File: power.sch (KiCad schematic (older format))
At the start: 14 parts

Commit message: Bom
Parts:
- removed BT?: Battery, symbol Battery
- C1: renamed from C?; footprint (none) -> Capacitors_SMD:C_1210
- C2: renamed from C?; value 100n 10V -> 100n 100V; footprint Capacitors_SMD:C_0402 -> Capacitors_SMD:C_0805; Rating 10V -> 100V
- C3: renamed from C?; footprint (none) -> Capacitors_SMD:C_1206
- D3: renamed from D?; footprint (none) -> Diodes_SMD:SOD-123
- R2: renamed from R?; footprint (none) -> Resistors_SMD:R_0402
- R3: renamed from R?; value 28k -> 28k 1%; footprint (none) -> Resistors_SMD:R_0402
- R4: renamed from R?; value 8.45k -> 8.45k 1%; footprint (none) -> Resistors_SMD:R_0402
- gave numbers to parts that had none: 6
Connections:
- net labels removed: VBAT
- wire segments 33 -> 31
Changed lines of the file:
@@
 $EndDescr
 $Comp
-L VIN #PWR?
+L VIN #PWR01
 U 1 1 562BB258
 P 750 1250
-F 0 "#PWR?" H 750 1100 50  0001 C CNN
+F 0 "#PWR01" H 750 1100 50  0001 C CNN
 F 1 "VIN" H 750 1390 50  0000 C CNN
 F 2 "" H 750 1250 60  0000 C CNN
@@
 24 V
 $Comp
-L R R?
+L R R1
 U 1 1 5637DBF2
 P 1200 2450
-F 0 "R?" V 1280 2450 50  0000 C CNN
+F 0 "R1" V 1280 2450 50  0000 C CNN
 F 1 "100k" V 1200 2450 50  0000 C CNN
 F 2 "Resistors_SMD:R_1206" V 1130 2450 30  0001 C CNN
@@
 $EndComp
 $Comp
-L GND #PWR?
+L GND #PWR02
 U 1 1 5637DBF8
 P 1200 2900
-F 0 "#PWR?" H 1200 2650 50  0001 C CNN
+F 0 "#PWR02" H 1200 2650 50  0001 C CNN
 F 1 "GND" H 1200 2750 50  0000 C CNN
 F 2 "" H 1200 2900 60  0000 C CNN
@@
 $EndComp
 $Comp
-L ZENER D?
+L ZENER D2
 U 1 1 5637E04D
 P 1600 1750
-F 0 "D?" H 1600 1850 50  0000 C CNN
+F 0 "D2" H 1600 1850 50  0000 C CNN
 F 1 "10V" H 1600 1650 50  0000 C CNN
 F 2 "Diodes_SMD:SMA_Standard" H 1600 1750 60  0001 C CNN
@@
 $EndComp
 $Comp
-L Battery BT?
-U 1 1 57AF2EDA
-P 2650 6400
-F 0 "BT?" H 2768 6446 50  0000 L CNN
-F 1 "Battery" H 2768 6355 50  0000 L CNN
-F 2 "" V 2650 6440 50  0001 C CNN
-F 3 "" V 2650 6440 50  0000 C CNN
-	1    2650 6400
-	1    0    0    -1
-$EndComp
-$Comp
-L VBAT #PWR?
-U 1 1 57AF30BC
-P 2650 6000
-F 0 "#PWR?" H 2650 5850 50  0001 C CNN
-F 1 "VBAT" H 2650 6140 50  0000 C CNN
-F 2 "" H 2650 6000 60  0000 C CNN
-F 3 "" H 2650 6000 60  0000 C CNN
-	1    2650 6000
-	1    0    0    -1
-$EndComp
-$Comp
-L GND #PWR?
-U 1 1 57AF3133
-P 2650 6800
-F 0 "#PWR?" H 2650 6550 50  0001 C CNN
-F 1 "GND" H 2650 6650 50  0000 C CNN
-F 2 "" H 2650 6800 60  0000 C CNN
-F 3 "" H 2650 6800 60  0000 C CNN
-	1    2650 6800
-	1    0    0    -1
-$EndComp
-$Comp
-L TVS D?
+L TVS D1
 U 1 1 57AF3BB5
 P 850 2200
-F 0 "D?" V 804 2288 50  0000 L CNN
+F 0 "D1" V 804 2288 50  0000 L CNN
 F 1 "40.2V" V 895 2288 50  0000 L CNN
 F 2 "can-node:DO-214AC" H 850 2200 50  0001 C CNN
@@
 $EndComp
 $Comp
-L GND #PWR?
+L GND #PWR03
 U 1 1 57AF3EE9
 P 850 2900
-F 0 "#PWR?" H 850 2650 50  0001 C CNN
+F 0 "#PWR03" H 850 2650 50  0001 C CNN
 F 1 "GND" H 850 2750 50  0000 C CNN
 F 2 "" H 850 2900 60  0000 C CNN
@@
 	750  1400 950  1400
 Wire Wire Line
-	2650 6000 2650 6250
-Wire Wire Line
-	2650 6550 2650 6800
-Wire Wire Line
 	850  1900 850  1400
 Connection ~ 850  1400
@@
 	1350 1400 2900 1400
 $Comp
-L GND #PWR?
+L GND #PWR04
 U 1 1 57C23EF3
 P 4350 5750
-F 0 "#PWR?" H 4350 5500 50  0001 C CNN
+F 0 "#PWR04" H 4350 5500 50  0001 C CNN
 F 1 "GND" H 4350 5600 50  0000 C CNN
 F 2 "" H 4350 5750 60  0000 C CNN
@@
 $EndComp
 $Comp
-L GNDA #PWR?
+L GNDA #PWR05
 U 1 1 57C23EF9
 P 4700 5750
-F 0 "#PWR?" H 4700 5500 50  0001 C CNN
+F 0 "#PWR05" H 4700 5500 50  0001 C CNN
 F 1 "GNDA" H 4700 5600 50  0000 C CNN
 F 2 "" H 4700 5750 60  0000 C CNN
@@
 	4350 5750 4700 5750
 $Comp
-L +3.3V #PWR?
+L +3.3V #PWR06
 U 1 1 57C23F59
 P 4350 5400
-F 0 "#PWR?" H 4350 5250 50  0001 C CNN
+F 0 "#PWR06" H 4350 5250 50  0001 C CNN
 F 1 "+3.3V" H 4365 5573 50  0000 C CNN
 F 2 "" H 4350 5400 50  0000 C CNN
@@
 $EndComp
 $Comp
-L +3.3VADC #PWR?
+L +3.3VADC #PWR07
 U 1 1 57C23F9D
 P 4700 5400
-F 0 "#PWR?" H 4850 5350 50  0001 C CNN
+F 0 "#PWR07" H 4850 5350 50  0001 C CNN
 F 1 "+3.3VADC" H 4720 5543 50  0000 C CNN
 F 2 "" H 4700 5400 50  0000 C CNN
@@
 	4700 5450 4700 5400
 $Comp
-L DMP6023LSS Q?
+L DMP6023LSS Q1
 U 1 1 57C95065
 P 1150 1500
-F 0 "Q?" V 1450 1500 50  0000 C CNN
+F 0 "Q1" V 1450 1500 50  0000 C CNN
 F 1 "DMP6023LSS" V 1350 1500 50  0000 C CNN
 F 2 "can-node:DMP6023LSS" V 1100 1750 50  0001 C CIN
@@
 $EndComp
 $Comp
-L LMR16006 U?
+L LMR16006 U1
 U 1 1 57D41661
 P 3300 1700
-F 0 "U?" H 3300 2287 60  0000 C CNN
+F 0 "U1" H 3300 2287 60  0000 C CNN
 F 1 "LMR16006" H 3300 2181 60  0000 C CNN
-F 2 "" H 3300 1600 60  0000 C CNN
+F 2 "" H 3300 1600 60  0001 C CNN
 F 3 "" H 3300 1600 60  0000 C CNN
 	1    3300 1700
@@
 $EndComp
 $Comp
-L C C?
+L C C2
 U 1 1 57D41A9C
 P 3950 1400
-F 0 "C?" V 3698 1400 50  0000 C CNN
-F 1 "100n 10V" V 3789 1400 50  0000 C CNN
-F 2 "Capacitors_SMD:C_0402" H 3988 1250 50  0001 C CNN
+F 0 "C2" V 3698 1400 50  0000 C CNN
+F 1 "100n 100V" V 3789 1400 50  0000 C CNN
+F 2 "Capacitors_SMD:C_0805" H 3988 1250 50  0001 C CNN
 F 3 "" H 3950 1400 50  0000 C CNN
-F 4 "10V" V 3950 1400 60  0001 C CNN "Rating"
+F 4 "100V" V 3950 1400 60  0001 C CNN "Rating"
 	1    3950 1400
 	0    1    1    0
 $EndComp
 $Comp
-L D_Schottky D?
+L D_Schottky D3
 U 1 1 57D41C33
 P 4150 1800
-F 0 "D?" V 4104 1879 50  0000 L CNN
+F 0 "D3" V 4104 1879 50  0000 L CNN
 F 1 "0.57V 1A" V 4195 1879 50  0000 L CNN
-F 2 "" H 4150 1800 50  0000 C CNN
+F 2 "Diodes_SMD:SOD-123" H 4150 1800 50  0001 C CNN
 F 3 "" H 4150 1800 50  0000 C CNN
 	1    4150 1800
@@
 $EndComp
 $Comp
-L INDUCTOR L?
+L INDUCTOR L1
 U 1 1 57D41D41
 P 4550 1600
-F 0 "L?" V 4766 1600 50  0000 C CNN
+F 0 "L1" V 4766 1600 50  0000 C CNN
 F 1 "27µH 220mΩ" V 4675 1600 50  0000 C CNN
-F 2 "" H 4550 1600 50  0000 C CNN
+F 2 "" H 4550 1600 50  0001 C CNN
 F 3 "" H 4550 1600 50  0000 C CNN
 	1    4550 1600
@@
 $EndComp
 $Comp
-L C C?
+L C C3
 U 1 1 57D41E1E
 P 5350 1900
-F 0 "C?" H 5465 1946 50  0000 L CNN
+F 0 "C3" H 5465 1946 50  0000 L CNN
 F 1 "22µF" H 5465 1855 50  0000 L CNN
-F 2 "" H 5388 1750 50  0000 C CNN
+F 2 "Capacitors_SMD:C_1206" H 5388 1750 50  0001 C CNN
 F 3 "" H 5350 1900 50  0000 C CNN
 	1    5350 1900
@@
 $EndComp
 $Comp
-L R R?
+L R R3
 U 1 1 57D41F11
 P 4950 1800
-F 0 "R?" H 5020 1846 50  0000 L CNN
-F 1 "28k" H 5020 1755 50  0000 L CNN
-F 2 "" V 4880 1800 50  0000 C CNN
+F 0 "R3" H 5020 1846 50  0000 L CNN
+F 1 "28k 1%" H 5020 1755 50  0000 L CNN
+F 2 "Resistors_SMD:R_0402" V 4880 1800 50  0001 C CNN
 F 3 "" H 4950 1800 50  0000 C CNN
 	1    4950 1800
@@
 $EndComp
 $Comp
-L R R?
+L R R4
 U 1 1 57D41FE1
 P 4950 2200
-F 0 "R?" H 5020 2246 50  0000 L CNN
-F 1 "8.45k" H 5020 2155 50  0000 L CNN
-F 2 "" V 4880 2200 50  0000 C CNN
+F 0 "R4" H 5020 2246 50  0000 L CNN
+F 1 "8.45k 1%" H 5020 2155 50  0000 L CNN
+F 2 "Resistors_SMD:R_0402" V 4880 2200 50  0001 C CNN
 F 3 "" H 4950 2200 50  0000 C CNN
 	1    4950 2200
@@
 $EndComp
 $Comp
-L R R?
+L R R2
 U 1 1 57D4210A
 P 2750 1550
-F 0 "R?" H 2820 1596 50  0000 L CNN
+F 0 "R2" H 2820 1596 50  0000 L CNN
 F 1 "100k" H 2820 1505 50  0000 L CNN
-F 2 "" V 2680 1550 50  0000 C CNN
+F 2 "Resistors_SMD:R_0402" V 2680 1550 50  0001 C CNN
 F 3 "" H 2750 1550 50  0000 C CNN
 	1    2750 1550
@@
 $EndComp
 $Comp
-L C C?
+L C C1
 U 1 1 57D42289
 P 2350 1650
-F 0 "C?" H 2465 1696 50  0000 L CNN
+F 0 "C1" H 2465 1696 50  0000 L CNN
 F 1 "2.2µF" H 2465 1605 50  0000 L CNN
-F 2 "" H 2388 1500 50  0000 C CNN
+F 2 "Capacitors_SMD:C_1210" H 2388 1500 50  0001 C CNN
 F 3 "" H 2350 1650 50  0000 C CNN
 	1    2350 1650
@@
 	3700 1600 4250 1600
 $Comp
-L GND #PWR?
+L GND #PWR08
 U 1 1 57D426D3
 P 4150 2150
-F 0 "#PWR?" H 4150 1900 50  0001 C CNN
+F 0 "#PWR08" H 4150 1900 50  0001 C CNN
 F 1 "GND" H 4155 1977 50  0000 C CNN
 F 2 "" H 4150 2150 50  0000 C CNN
@@
 Connection ~ 4150 1600
 $Comp
-L GND #PWR?
+L GND #PWR09
 U 1 1 57D42BF3
 P 4950 2400
-F 0 "#PWR?" H 4950 2150 50  0001 C CNN
+F 0 "#PWR09" H 4950 2150 50  0001 C CNN
 F 1 "GND" H 4955 2227 50  0000 C CNN
 F 2 "" H 4950 2400 50  0000 C CNN
@@
 $EndComp
 $Comp
-L GND #PWR?
+L GND #PWR010
 U 1 1 57D42C55
 P 5350 2400
-F 0 "#PWR?" H 5350 2150 50  0001 C CNN
+F 0 "#PWR010" H 5350 2150 50  0001 C CNN
 F 1 "GND" H 5355 2227 50  0000 C CNN
 F 2 "" H 5350 2400 50  0000 C CNN
@@
 $EndComp
 $Comp
-L GND #PWR?
+L GND #PWR011
 U 1 1 57D42CB7
 P 2900 2400
-F 0 "#PWR?" H 2900 2150 50  0001 C CNN
+F 0 "#PWR011" H 2900 2150 50  0001 C CNN
 F 1 "GND" H 2905 2227 50  0000 C CNN
 F 2 "" H 2900 2400 50  0000 C CNN
@@
 $EndComp
 $Comp
-L GND #PWR?
+L GND #PWR012
 U 1 1 57D42E3B
 P 2350 1850
-F 0 "#PWR?" H 2350 1600 50  0001 C CNN
+F 0 "#PWR012" H 2350 1600 50  0001 C CNN
 F 1 "GND" H 2355 1677 50  0000 C CNN
 F 2 "" H 2350 1850 50  0000 C CNN
@@
 	5350 2400 5350 2050
 $Comp
-L +3.3V #PWR?
+L +3.3V #PWR013
 U 1 1 57D43B9E
 P 5950 1350
-F 0 "#PWR?" H 5950 1200 50  0001 C CNN
+F 0 "#PWR013" H 5950 1200 50  0001 C CNN
 F 1 "+3.3V" H 5965 1523 50  0000 C CNN
 F 2 "" H 5950 1350 50  0000 C CNN

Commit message: Finish BOM, assign and add packages, set connectors, minor changes
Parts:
- D1: footprint can-node:DO-214AC -> Diodes_SMD:SMA_Handsoldering
- D2: footprint Diodes_SMD:SMA_Standard -> Diodes_SMD:SMA_Handsoldering
- L1: footprint (none) -> CAN_Node:SDE0604A_HandSoldering
- Q1: footprint can-node:DMP6023LSS -> CAN_Node:DMP6023LSS
- U1: footprint (none) -> TO_SOT_Packages_SMD:TSOT-6-MK06A_Handsoldering
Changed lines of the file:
@@
 F 0 "D2" H 1600 1850 50  0000 C CNN
 F 1 "10V" H 1600 1650 50  0000 C CNN
-F 2 "Diodes_SMD:SMA_Standard" H 1600 1750 60  0001 C CNN
+F 2 "Diodes_SMD:SMA_Handsoldering" H 1600 1750 60  0001 C CNN
 F 3 "http://www.onsemi.com/pub_link/Collateral/MM3Z2V4T1-D.PDF" H 1600 1750 60  0001 C CNN
 F 4 "ON Semiconductor 1SMA5925BT3G" H 1600 1750 60  0001 C CNN "Device"
@@
 F 0 "D1" V 804 2288 50  0000 L CNN
 F 1 "40.2V" V 895 2288 50  0000 L CNN
-F 2 "can-node:DO-214AC" H 850 2200 50  0001 C CNN
+F 2 "Diodes_SMD:SMA_Handsoldering" H 850 2200 50  0001 C CNN
 F 3 "http://www.vishay.com/docs/88367/p4sma.pdf" H 850 2200 50  0001 C CNN
 F 4 "P4SMA47CA" V 1100 2200 60  0000 C CNN "Part"
@@
 F 0 "Q1" V 1450 1500 50  0000 C CNN
 F 1 "DMP6023LSS" V 1350 1500 50  0000 C CNN
-F 2 "can-node:DMP6023LSS" V 1100 1750 50  0001 C CIN
+F 2 "CAN_Node:DMP6023LSS" V 1100 1750 50  0001 C CIN
 F 3 "" H 1150 1500 50  0000 L CNN
 	1    1150 1500
@@
 F 0 "U1" H 3300 2287 60  0000 C CNN
 F 1 "LMR16006" H 3300 2181 60  0000 C CNN
-F 2 "" H 3300 1600 60  0001 C CNN
+F 2 "TO_SOT_Packages_SMD:TSOT-6-MK06A_Handsoldering" H 3300 1600 60  0001 C CNN
 F 3 "" H 3300 1600 60  0000 C CNN
 	1    3300 1700
@@
 F 0 "L1" V 4766 1600 50  0000 C CNN
 F 1 "27µH 220mΩ" V 4675 1600 50  0000 C CNN
-F 2 "" H 4550 1600 50  0001 C CNN
+F 2 "CAN_Node:SDE0604A_HandSoldering" H 4550 1600 50  0001 C CNN
 F 3 "" H 4550 1600 50  0000 C CNN
 	1    4550 1600

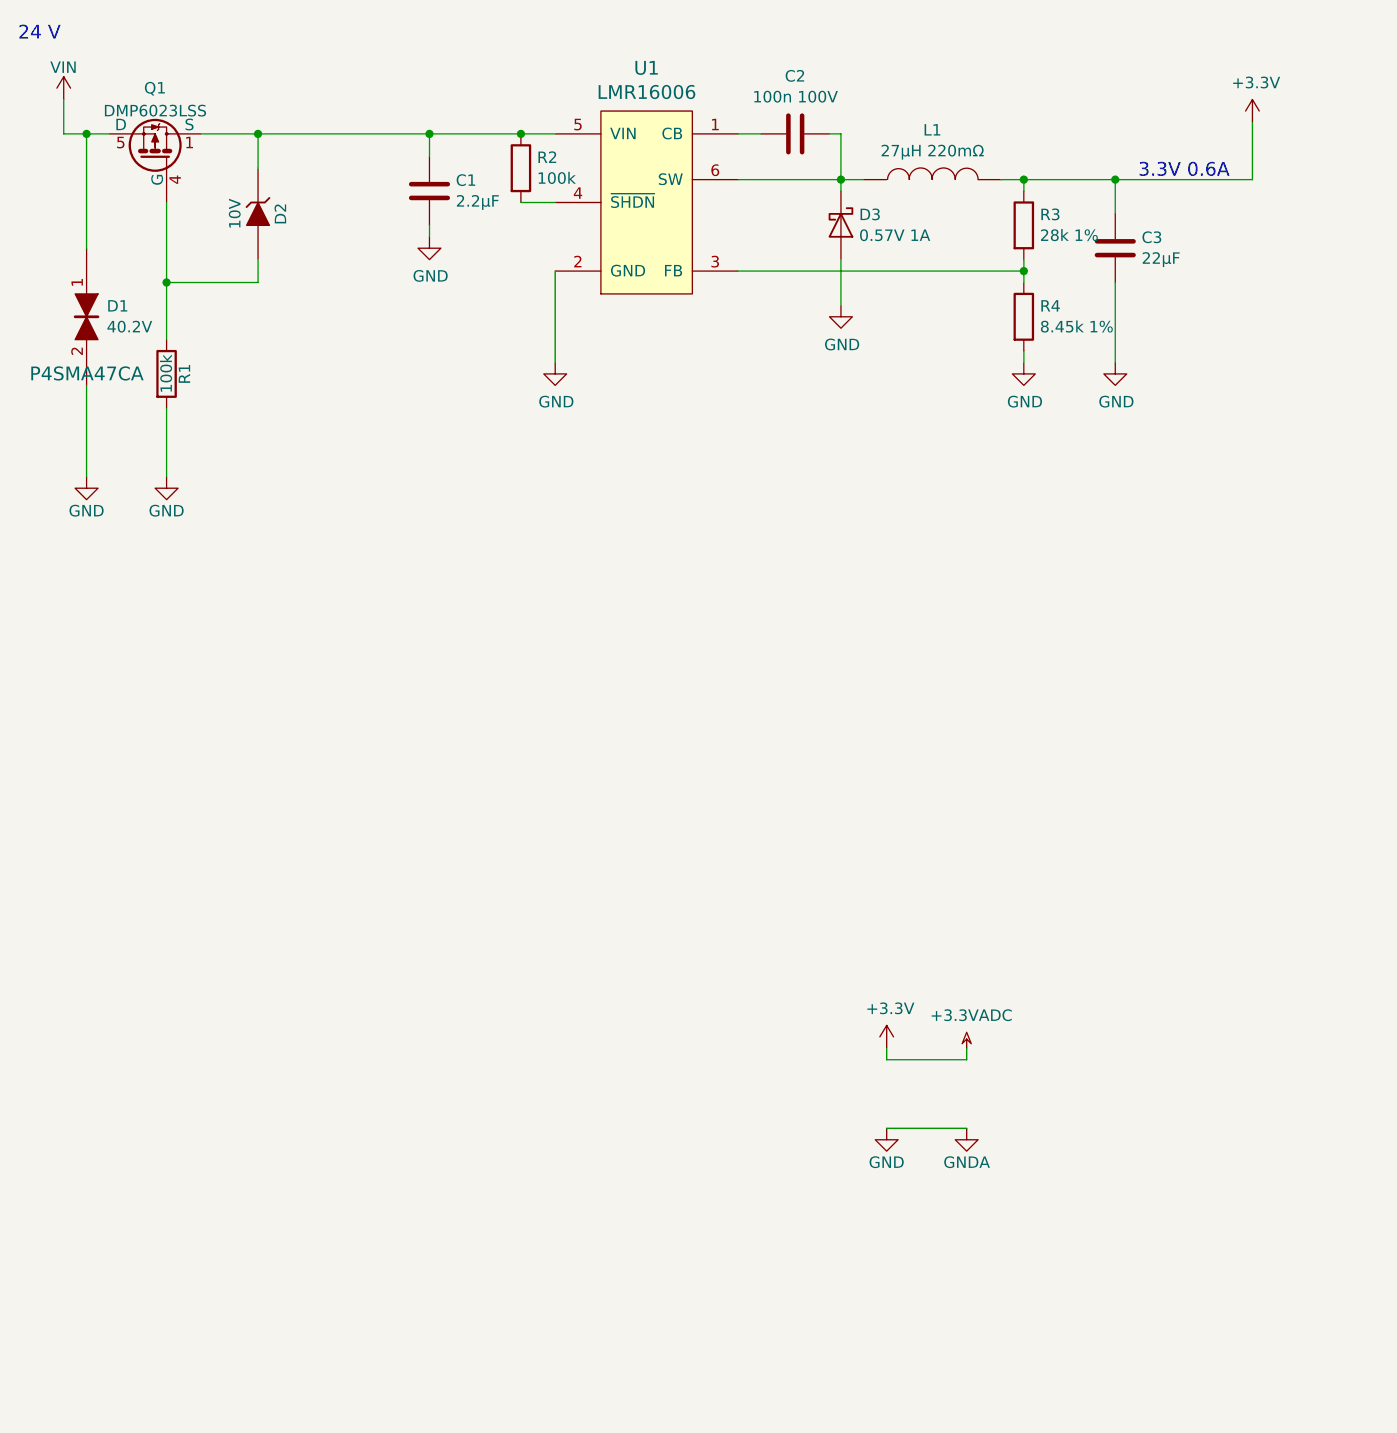
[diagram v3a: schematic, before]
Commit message: Some modifications to schematic, BOM, start releayout
- add LED display
- change crystal for RTC
- use components that are available at some distributors
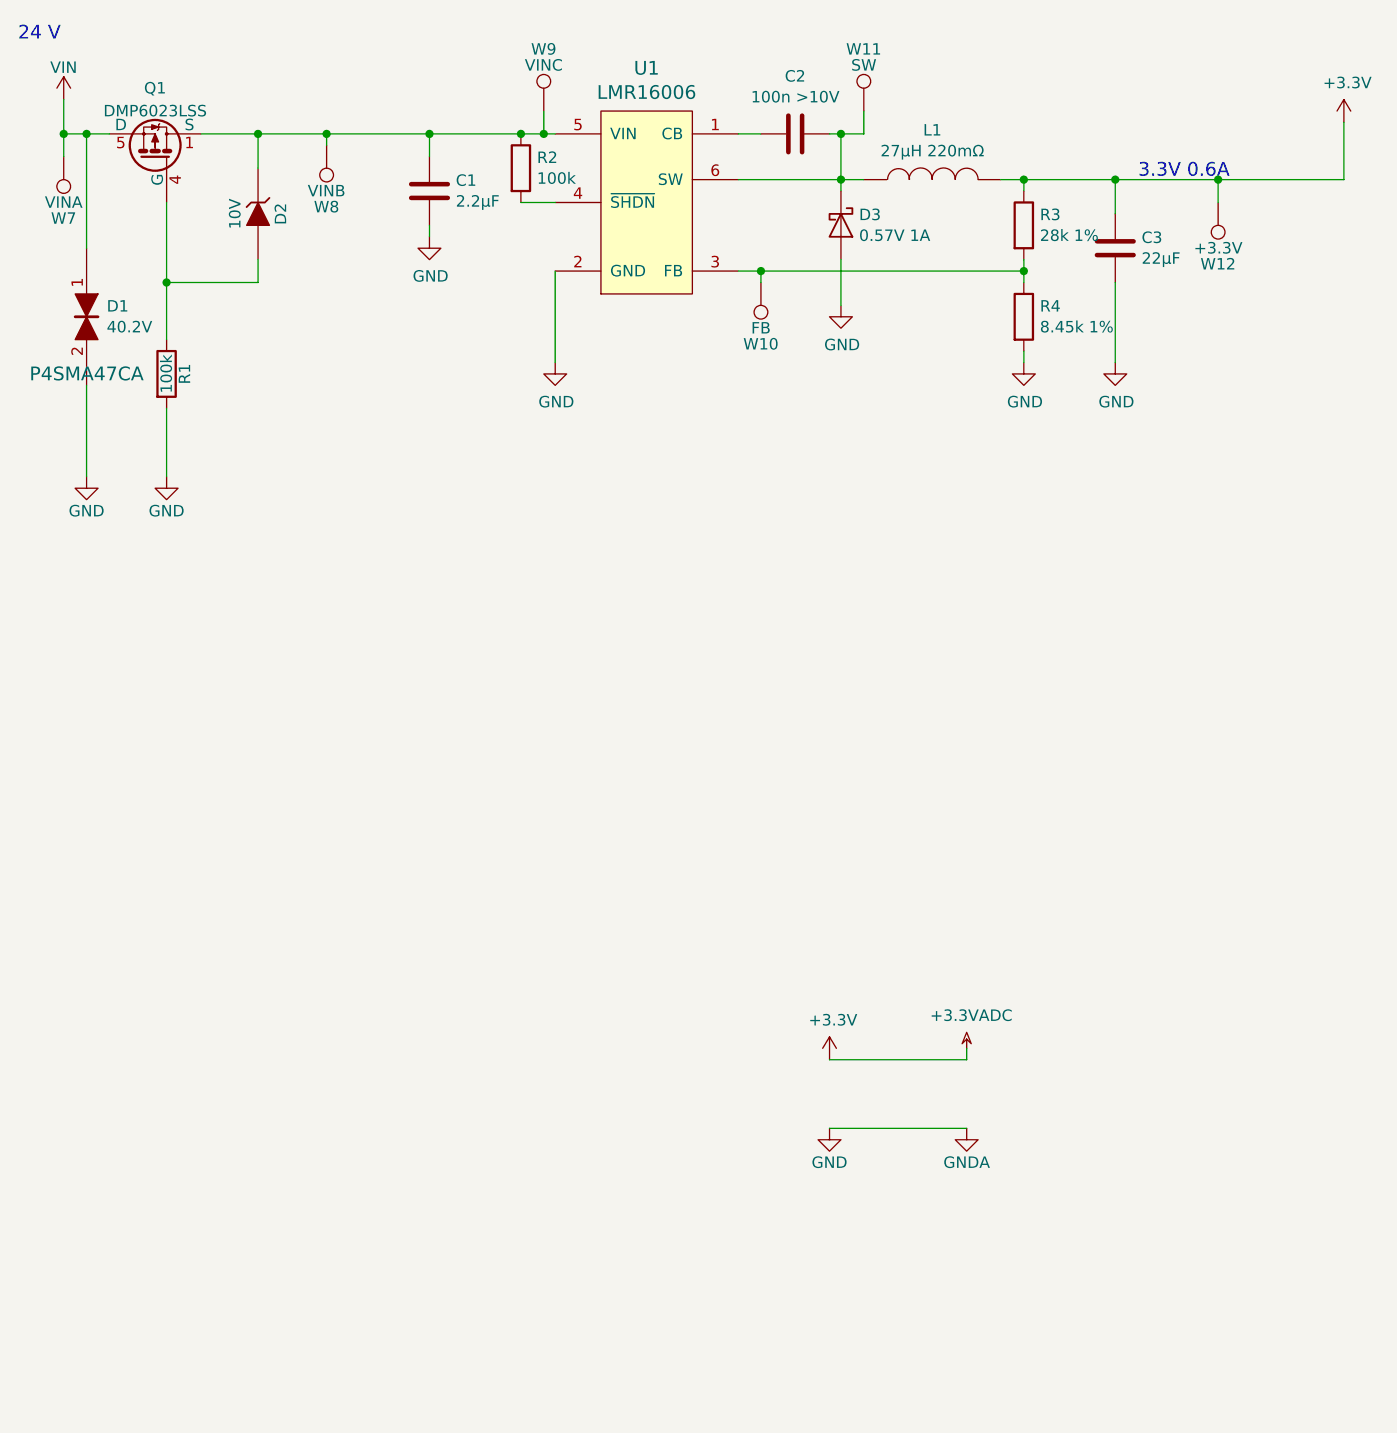
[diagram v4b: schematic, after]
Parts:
- added W10: FB, can-node:Measurement_Point_tiny, symbol TEST_1P
- added W11: SW, can-node:Measurement_Point_tiny, symbol TEST_1P
- added W12: +3.3V, can-node:Measurement_Point_tiny, symbol TEST_1P
- added W7: VINA, can-node:Measurement_Point_tiny, symbol TEST_1P
- added W8: VINB, can-node:Measurement_Point_tiny, symbol TEST_1P
- added W9: VINC, can-node:Measurement_Point_tiny, symbol TEST_1P
- C2: value 100n 100V -> 100n >10V
- L1: footprint CAN_Node:SDE0604A_HandSoldering -> can-node:SDE0604A_HandSoldering
- Q1: footprint CAN_Node:DMP6023LSS -> can-node:DMP6023LSS
- U1: footprint TO_SOT_Packages_SMD:TSOT-6-MK06A_Handsoldering -> can-node:TI-DDC
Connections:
- net +3.3VADC: now also W12.1
- net VIN: now also W7.1
- net at C1.1, D2.1 (K), Q1.1 (S)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: now also W8.1, W9.1
- net at R3.2, R4.1, U1.3 (FB): now also W10.1
- net at C2.1, D3.1 (K), L1.1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: now also W11.1
